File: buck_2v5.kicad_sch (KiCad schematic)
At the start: 16 parts, among them U2 XTPS564257DRLR

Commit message: CuPhy: adding ports
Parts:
- removed R5: 47K, Resistor_SMD:R_0805_2012Metric_Pad1.20x1.40mm_HandSolder, symbol Device:R
- removed R6: 20K, Resistor_SMD:R_0805_2012Metric_Pad1.20x1.40mm_HandSolder, symbol Device:R
- renumbered C25 to C79, C27 to C80, C74 to C81, C31 to C82, C28 to C83, C29 to C84, C30 to C85, L2 to L5, R7 to R19, R8 to R20, TP4 to TP13, TP5 to TP14, TP6 to TP15, U2 to U5

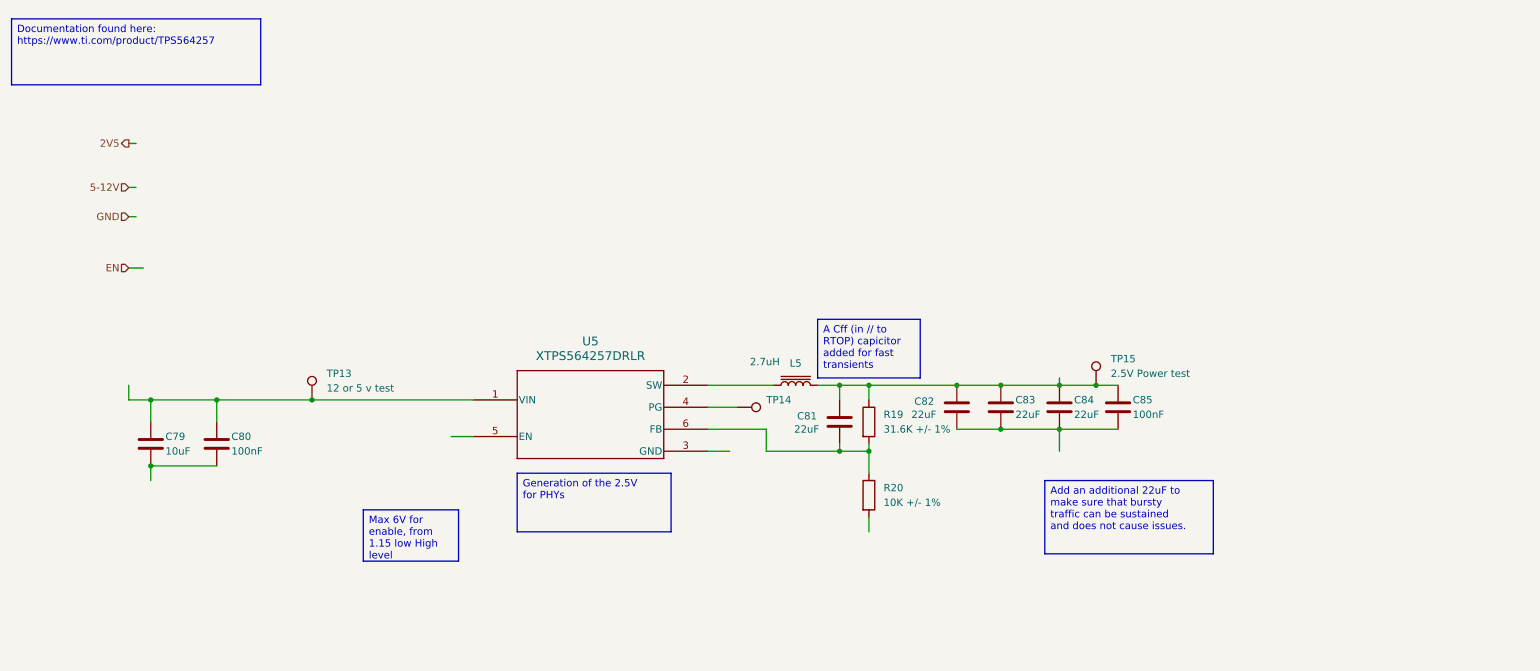
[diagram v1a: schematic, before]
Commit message: schematics: fixing the voltage rail and updating the files
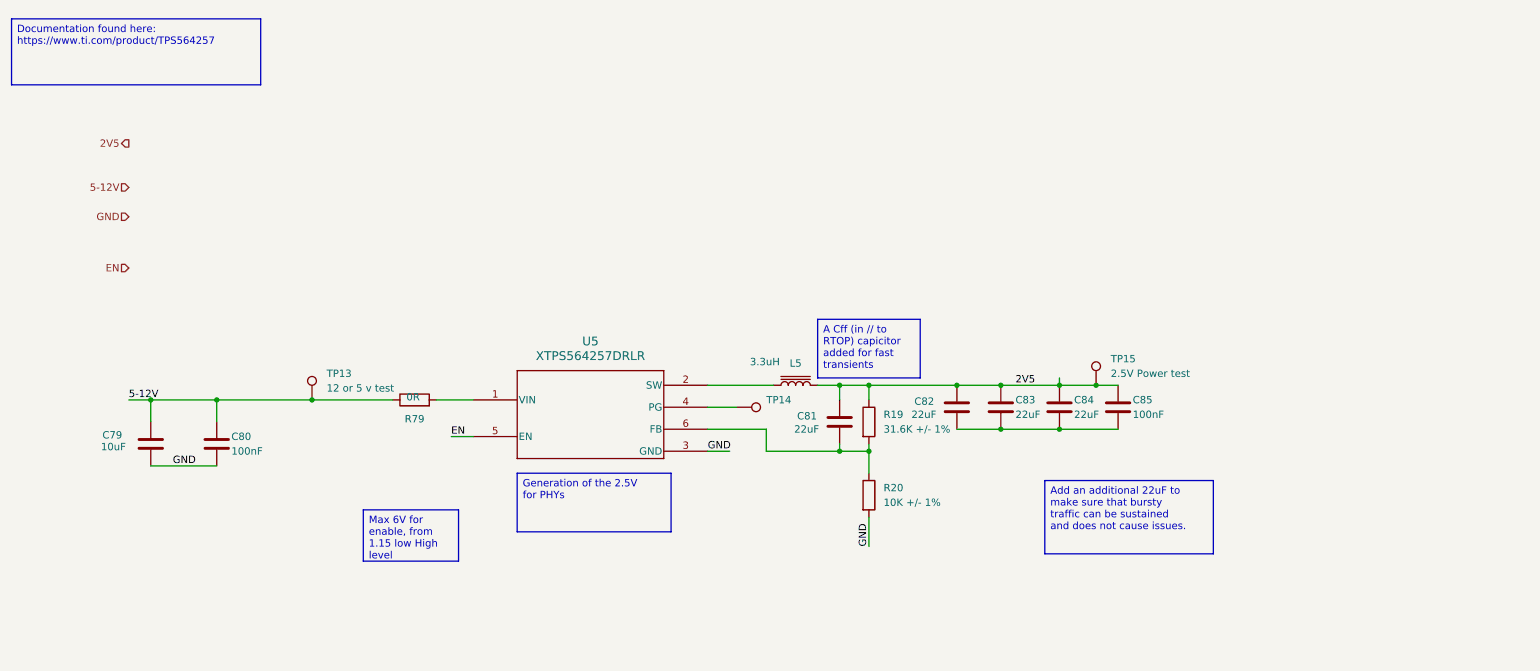
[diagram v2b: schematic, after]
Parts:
- added R79: 0R, KL_Footprints:R_2512, symbol KL_R:R_0R_2W_5_2512
- L5: value 2.7uH -> 3.3uH
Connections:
- net 2V5: now also C81.1, C82.1, C83.1, C84.1, C85.1, L5.2, R19.1, TP15.1
- net 5-12V: now also C79.1, C80.1, TP13.1, R79.1
- net EN: now also U5.5 (EN)
- net GND: now also C79.2, C80.2, R20.2, U5.3 (GND)
- new net: R79.2, U5.1 (VIN)

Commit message: switch: finished 1st version
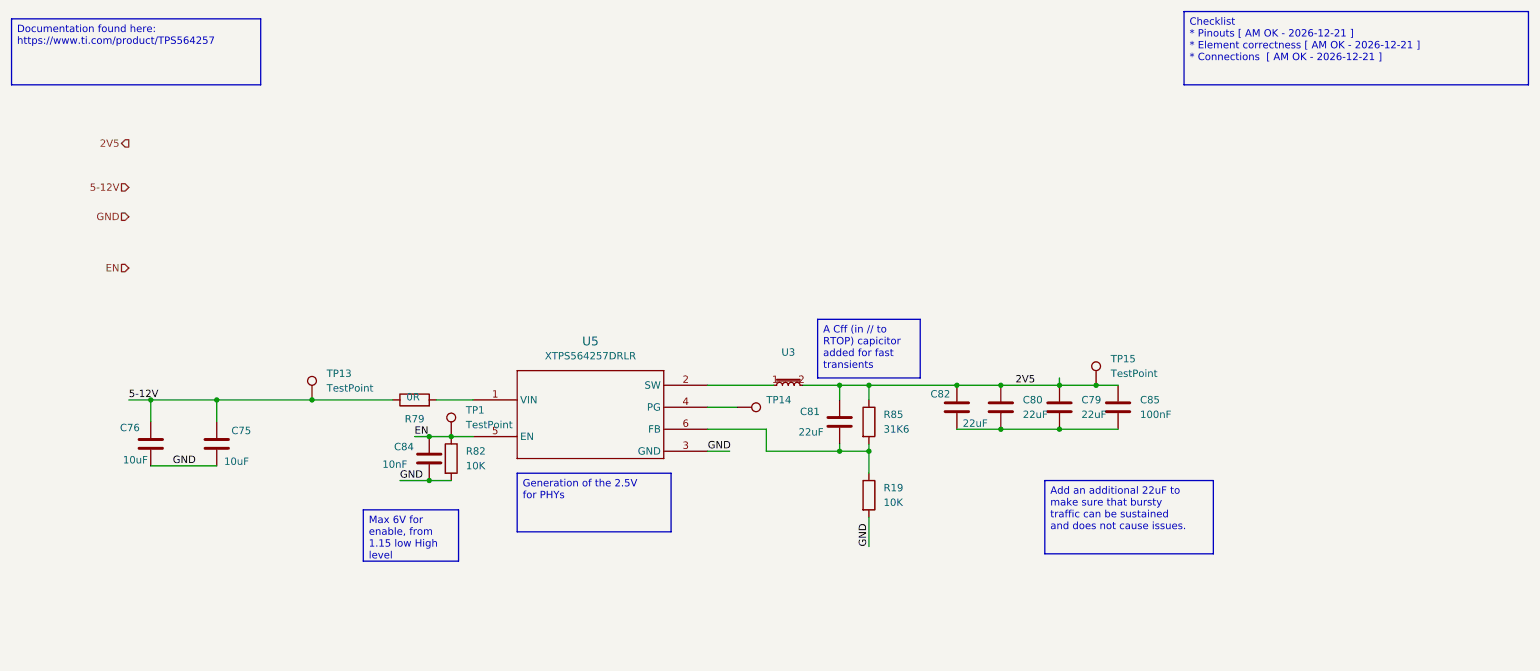
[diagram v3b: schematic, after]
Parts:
- removed C79: 10uF, Capacitor_SMD:C_0805_2012Metric_Pad1.18x1.45mm_HandSolder, symbol Device:C
- removed C80, C85: 100nF, Capacitor_SMD:C_0805_2012Metric_Pad1.18x1.45mm_HandSolder, symbol Device:C
- removed C81, C82, C83, C84: 22uF, Capacitor_SMD:C_0805_2012Metric_Pad1.18x1.45mm_HandSolder, symbol Device:C
- removed L5: 3.3uH, symbol Device:L_Iron
- removed R19: 31.6K +/- 1%, Resistor_SMD:R_0805_2012Metric_Pad1.20x1.40mm_HandSolder, symbol Device:R
- removed R20: 10K +/- 1%, Resistor_SMD:R_0805_2012Metric_Pad1.20x1.40mm_HandSolder, symbol Device:R
- added C75, C76: 10uF, KL:C_0603, symbol KL_C:C_10uF_25V_X5R_0603_20
- added C79, C80, C81, C82: 22uF, KL:C_0603, symbol KL_C:C_22uF_10V_X5R_0603_20
- added C84: 10nF, KL:C_0603, symbol KL_C:C_10nF_25V_X7R_0603_20
- added C85: 100nF, KL:C_0603, symbol KL_C:C_100nF_10V_X7R_0603_10
- added R19: 10K, KL:R_0603, symbol KL_R:R_10K_100mW_1_0603
- added R82: 10K, KL:R_0603, symbol KL_R:R_10K_100mW_5_0603
- added R85: 31K6, KL:R_0603, symbol KL_R:R_31K6_125mW_1_0603
- added TP1: TestPoint, symbol Connector:TestPoint
- added U3: ~, KL:L_3u3_EXLA1V0603, symbol KL_L:L_3u3_8A
- TP13: value 12 or 5 v test -> TestPoint
- TP14: value 12v test -> TestPoint
- TP15: value 2.5V Power test -> TestPoint
- U5: footprint TPS564242DRLR_TEX -> KL:SOT-563; symbol tps5642:XTPS564257DRLR -> KL_IC_Power:TI_TPS564357DRLR; Digikey (none) -> 296-TPS564257DRLRCT-ND; LSCS (none) -> C19272233; Mouser (none) -> 595-TPS564257DRLR
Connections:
- net 2V5: now also C79.1, C80.1, C81.1, C82.1, C85.1, R85.1, U3.2
- net 5-12V: now also C75.1, C76.1
- net EN: now also C84.1, R82.1, TP1.1
- net GND: now also C75.2, C76.2, C84.2, R19.2, R82.2
- net at U5.2 (SW): now also U3.1
- net at U5.6 (FB): now also C81.2, R19.1, R85.2
- new net: C79.2, C80.2, C82.2, C85.2
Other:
- company: Kebag-Logic <contact@kebag-logic.com -> Kebag-Logic <contact@kebag-logic.com>
- title: 2V5 Buck voltage convertion -> Switch 2.5V Power Rail

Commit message: minor footprint fixing
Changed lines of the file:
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@@
 			)
 		)
-		(property "Datasheet" "https://www.ti.com/lit/gpn/tps564257"
+		(property "Datasheet" ""
 			(at 120.65 80.01 0)
 			(effects
@@
 		(fields_autoplaced yes)
 		(property "Reference" "TP14"
-			(at 151.13 82.5499 90)
+			(at 151.13 83.8199 90)
 			(effects
 				(font
@@
 		(fields_autoplaced yes)
 		(property "Reference" "U3"
-			(at 154.94 74.295 0)
+			(at 154.94 73.66 0)
 			(effects
 				(font
@@
 		)
 		(property "Value" "~"
-			(at 154.94 76.835 0)
-			(effects
-				(font
+			(at 154.94 76.2 0)
+			(effects
+				(font

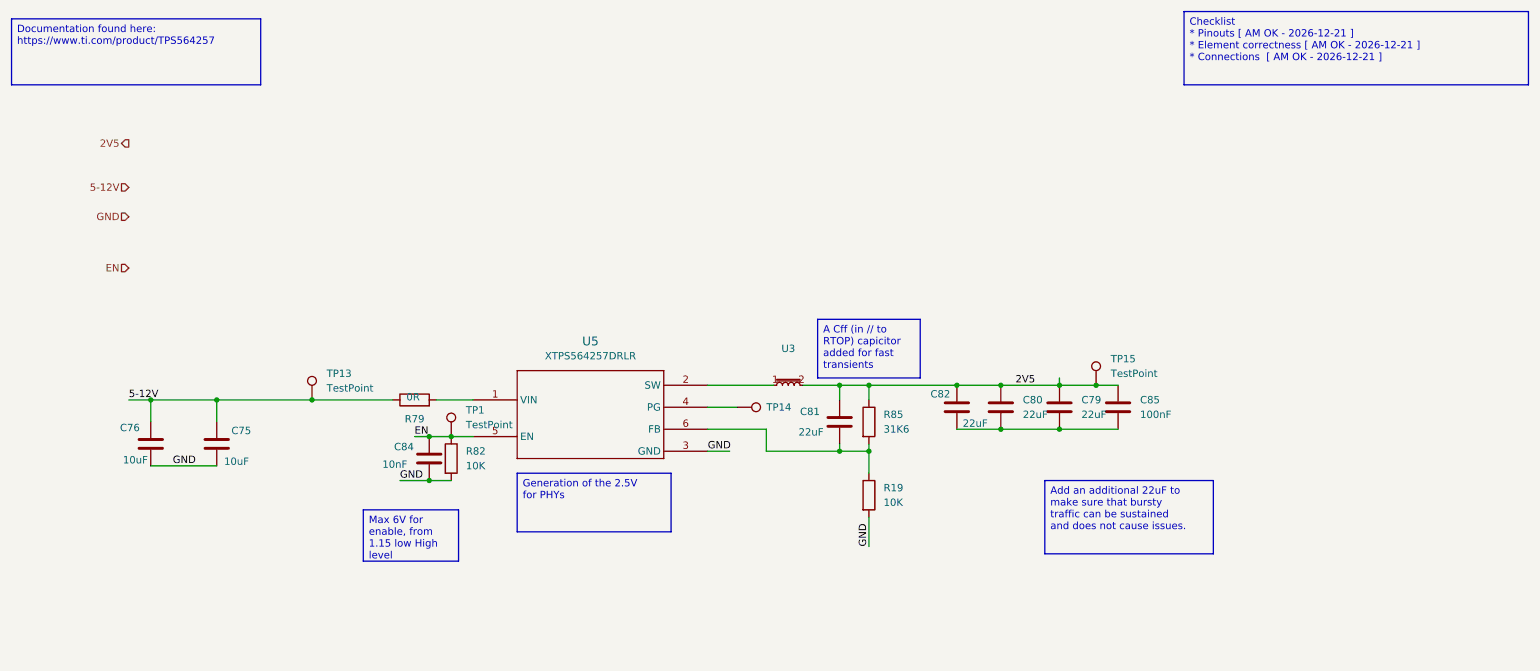
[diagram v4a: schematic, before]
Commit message: review of +2V5 converter
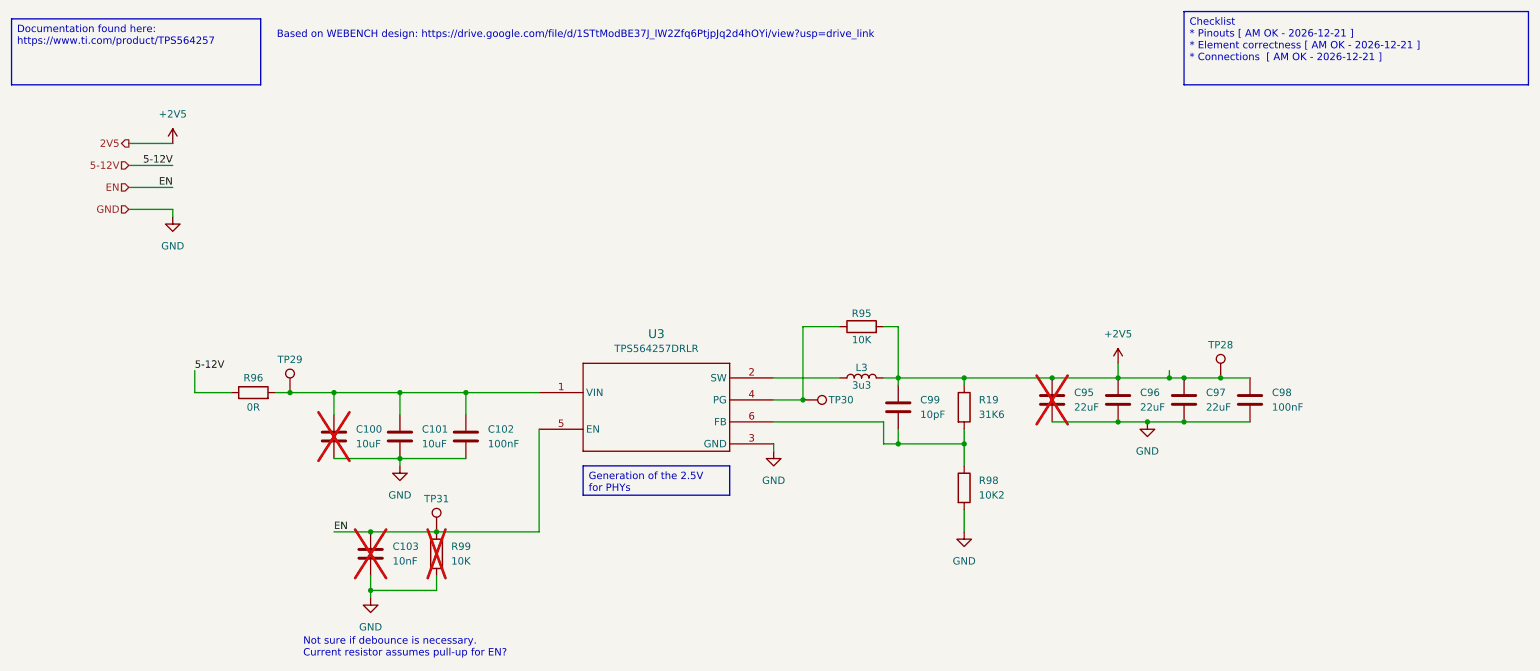
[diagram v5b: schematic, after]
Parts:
- removed C75, C76: 10uF, KL:C_0603, symbol KL_C:C_10uF_25V_X5R_0603_20
- removed C79, C80, C81, C82: 22uF, KL:C_0603, symbol KL_C:C_22uF_10V_X5R_0603_20
- removed C84: 10nF, KL:C_0603, symbol KL_C:C_10nF_25V_X7R_0603_20
- removed C85: 100nF, KL:C_0603, symbol KL_C:C_100nF_10V_X7R_0603_10
- removed R19: 10K, KL:R_0603, symbol KL_R:R_10K_100mW_1_0603
- removed R79: 0R, KL_Footprints:R_2512, symbol KL_R:R_0R_2W_5_2512
- removed R82: 10K, KL:R_0603, symbol KL_R:R_10K_100mW_5_0603
- removed R85: 31K6, KL:R_0603, symbol KL_R:R_31K6_125mW_1_0603
- removed TP1, TP13, TP14, TP15: TestPoint, symbol Connector:TestPoint
- removed U3: ~, KL:L_3u3_EXLA1V0603, symbol KL_L:L_3u3_8A
- removed U5: XTPS564257DRLR, KL:SOT-563, symbol KL_IC_Power:TI_TPS564357DRLR
- added C100, C101: 10uF, KL:C_0603, symbol KL_C:C_10uF_25V_X5R_0603_20
- added C102: 100nF, KL:C_0603, symbol KL_C:C_100nF_16V_X7R_0603_10
- added C103: 10nF, KL:C_0603, symbol KL_C:C_10nF_25V_X7R_0603_20
- added C95, C96, C97: 22uF, KL:C_0603, symbol KL_C:C_22uF_10V_X5R_0603_20
- added C98: 100nF, KL:C_0603, symbol KL_C:C_100nF_10V_X7R_0603_10
- added C99: 10pF, Capacitor_SMD:C_0201_0603Metric, symbol KL_C:C_10pF_25V_C0G_0603_5
- added L3: 3u3, KL:L_3u3_EXLA1V0603, symbol KL_L:L_3u3_8A
- added R19: 31K6, KL_Footprints:C_0603, symbol KL_R:R_31K6_125mW_1_0603
- added R95: 10K, KL_Footprints:C_0603, symbol KL_R:R_10K_100mW_5_0603
- added R96: 0R, KL_Footprints:R_2512, symbol KL_R:R_0R_2W_5_2512
- added R98: 10K2, KL:R_0603, symbol KL_R:R_10K2_100mW_1_0603
- added R99: 10K, KL:R_0603, symbol KL_R:R_10K_100mW_5_0603
- added TP28, TP29, TP30, TP31: ~, Connector_PinHeader_2.54mm:PinHeader_1x01_P2.54mm_Vertical, symbol KL_TP:TestPoint
- added U3: TPS564257DRLR, KL:SOT-563, symbol KL_IC_Power:TI_TPS564357DRLR
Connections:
- net 5-12V: now also R96.1
- net EN: now also C103.1, R99.1, TP31.1, U3.5 (EN)
- net GND: now also C100.2, C101.2, C102.2, C103.2, C95.2, C96.2, C97.2, C98.2, R98.2, R99.2, U3.3 (GND)
- new net: C100.1, C101.1, C102.1, R96.2, TP29.1, U3.1 (VIN)
- new net: C99.2, R19.2, R98.1, U3.6 (FB)
- new net: R95.1, TP30.1, U3.4 (PG)
- new net: L3.1, U3.2 (SW)
- new net +2V5: C95.1, C96.1, C97.1, C98.1, C99.1, L3.2, R19.1, R95.2, TP28.1
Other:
- note added: "Based on WEBENCH design: https://drive.google.com/file/d/1STtModBE37J_lW2Zfq6PtjpJq2d4hOYi/view?usp=drive_link"
- note added: "Not sure if debounce is necessary. Current resistor assumes pull-up for EN?"
